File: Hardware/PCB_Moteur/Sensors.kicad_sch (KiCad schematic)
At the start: 19 parts, among them J18 Conn_01x04_Socket, J19 Conn_01x04_Socket, U7 INA125UA/2K5, U8 INA125UA/2K5, U9 MAX6612MXK

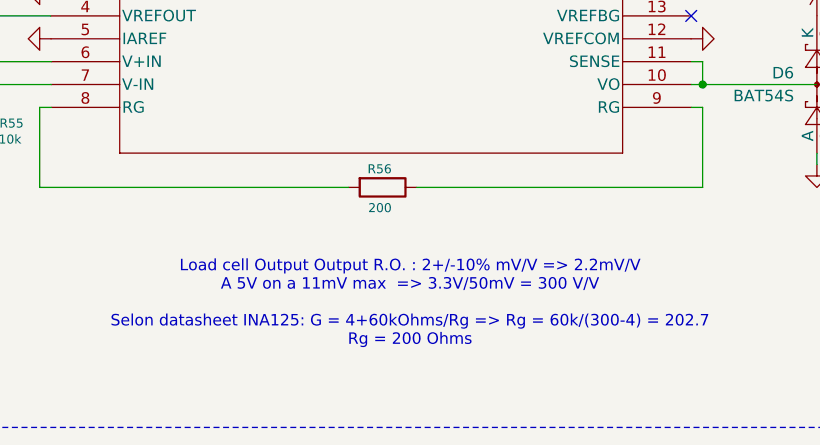
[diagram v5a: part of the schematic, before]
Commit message: wip : minor corrections and fix footprints except connectors
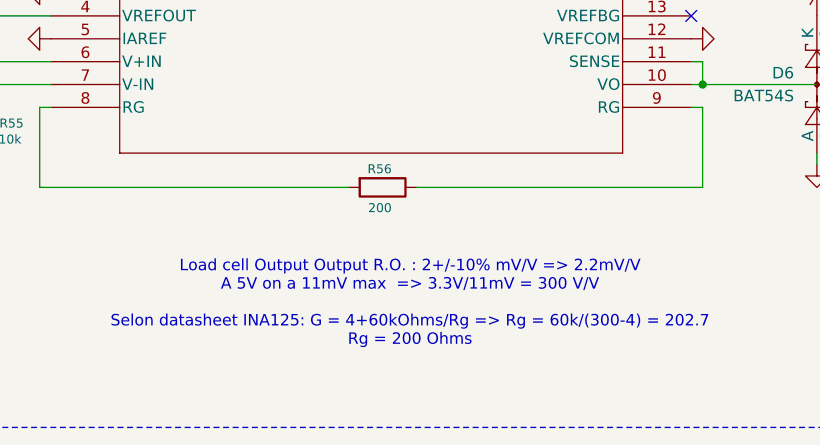
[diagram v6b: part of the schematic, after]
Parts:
- C44, C45, C46, C47, C48, C49: footprint (none) -> Capacitor_SMD:C_0805_2012Metric
- U7, U8: footprint D16 -> Package_SO:SOIC-16_3.9x9.9mm_P1.27mm
- U9: footprint MAX6612MXK:SOT65P210X110-5N -> Package_TO_SOT_SMD:SOT-353_SC-70-5
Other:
- note added: "Load cell Output Output R.O. : 2+/-10% mV/V => 2.2mV/V A 5V on a 11mV max => 3.3V/11mV = 300 V/V Selon datasheet INA125: G = 4+60kOhms/Rg => Rg = 60k/(300-4) = 202.7 Rg = 200 Ohms"
- note removed: "Load cell Output Output R.O. : 2+/-10% mV/V => 2.2mV/V A 5V on a 11mV max => 3.3V/50mV = 300 V/V Selon datasheet INA125: G = 4+60kOhms/Rg => Rg = 60k/(300-4) = 202.7 Rg = 200 Ohms"
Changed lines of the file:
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@@
 		)
 	)
-	(text "Load cell Output Output R.O. : 2+/-10% mV/V => 2.2mV/V\nA 5V on a 11mV max  => 3.3V/50mV = 300 V/V\n\nSelon datasheet INA125: G = 4+60kOhms/Rg => Rg = 60k/(300-4) = 202.7\nRg = 200 Ohms"
+	(text "Load cell Output Output R.O. : 2+/-10% mV/V => 2.2mV/V\nA 5V on a 11mV max  => 3.3V/11mV = 300 V/V\n\nSelon datasheet INA125: G = 4+60kOhms/Rg => Rg = 60k/(300-4) = 202.7\nRg = 200 Ohms"
 		(exclude_from_sim no)
 		(at 81.788 165.354 0)
@@
 			)
 		)
-		(property "Footprint" ""
+		(property "Footprint" "Capacitor_SMD:C_0805_2012Metric"
 			(at 140.6652 73.66 0)
 			(effects
@@
 			)
 		)
-		(property "Footprint" ""
+		(property "Footprint" "Capacitor_SMD:C_0805_2012Metric"
 			(at 266.7 33.3248 0)
 			(effects
@@
 			)
 		)
-		(property "Footprint" ""
+		(property "Footprint" "Capacitor_SMD:C_0805_2012Metric"
 			(at 258.7752 48.26 0)
 			(effects
@@
 			)
 		)
-		(property "Footprint" "MAX6612MXK:SOT65P210X110-5N"
+		(property "Footprint" "Package_TO_SOT_SMD:SOT-353_SC-70-5"
 			(at 240.03 44.45 0)
 			(effects
@@
 			)
 		)
-		(property "Footprint" ""
+		(property "Footprint" "Capacitor_SMD:C_0805_2012Metric"
 			(at 143.2052 148.59 0)
 			(effects
@@
 			)
 		)
-		(property "Footprint" "D16"
+		(property "Footprint" "Package_SO:SOIC-16_3.9x9.9mm_P1.27mm"
 			(at 41.91 125.73 0)
 			(effects
@@
 			)
 		)
-		(property "Footprint" ""
+		(property "Footprint" "Capacitor_SMD:C_0805_2012Metric"
 			(at 34.29 45.4152 0)
 			(effects
@@
 			)
 		)
-		(property "Footprint" "D16"
+		(property "Footprint" "Package_SO:SOIC-16_3.9x9.9mm_P1.27mm"
 			(at 43.18 50.8 0)
 			(effects
@@
 			)
 		)
-		(property "Footprint" ""
+		(property "Footprint" "Capacitor_SMD:C_0805_2012Metric"
 			(at 33.02 120.3452 0)
 			(effects

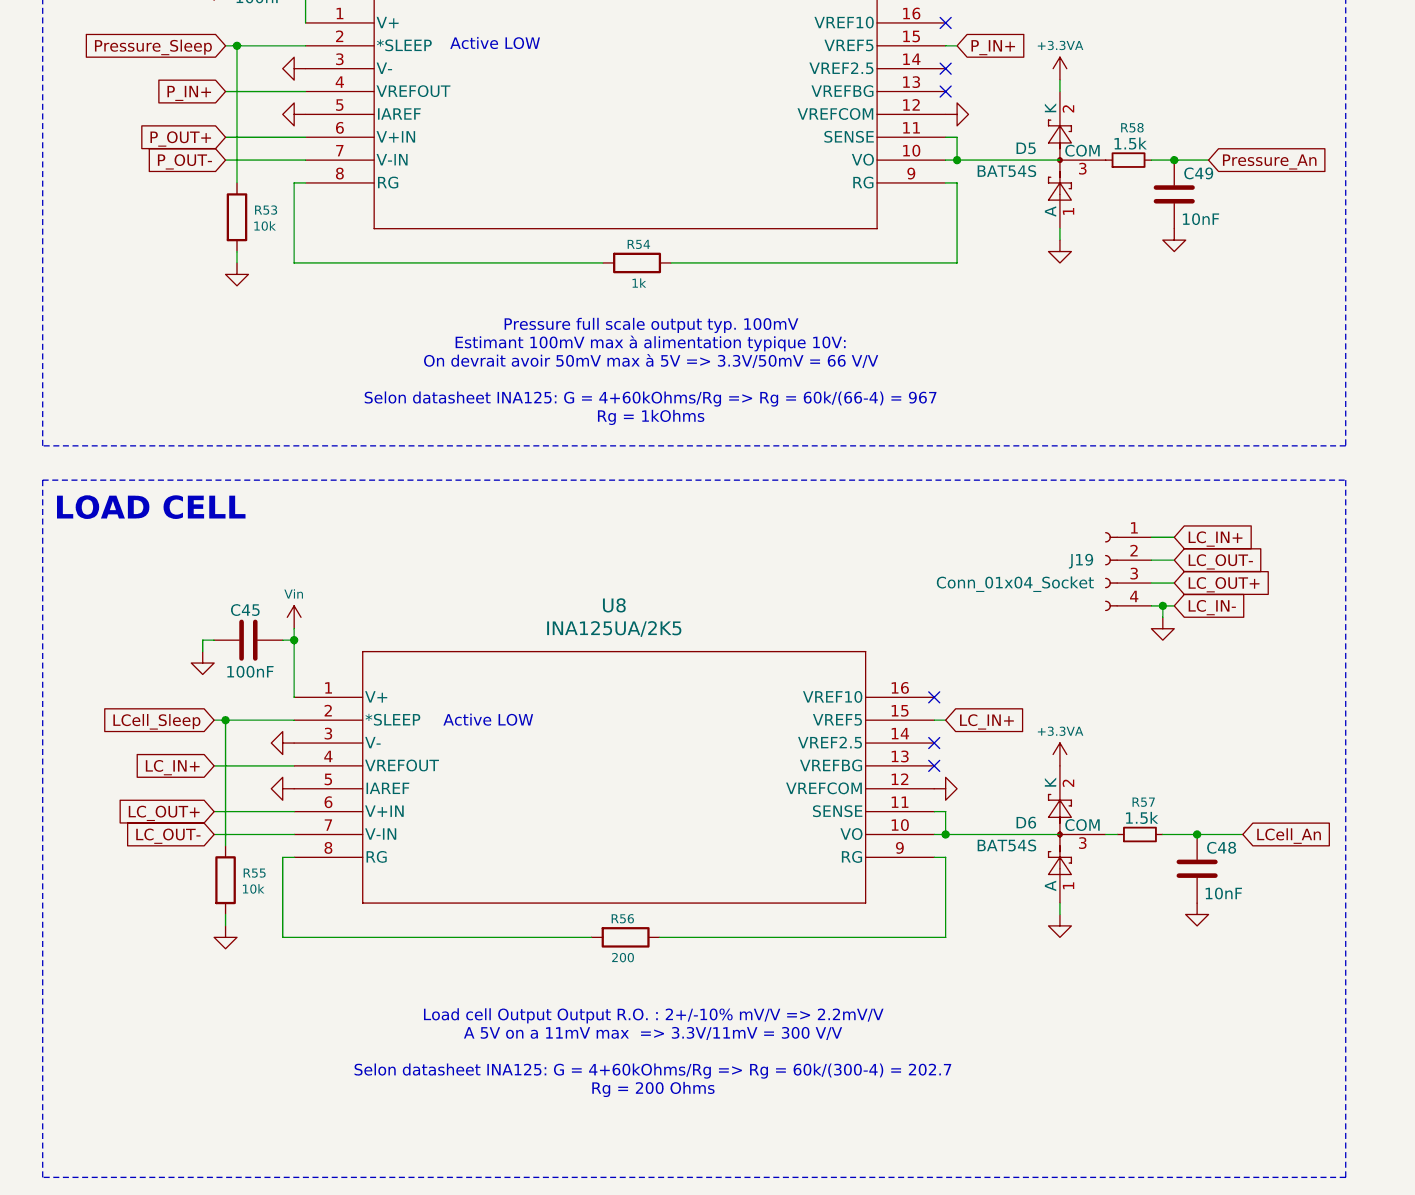
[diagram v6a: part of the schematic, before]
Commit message: fix: symbols refactorisation (footprint missing)
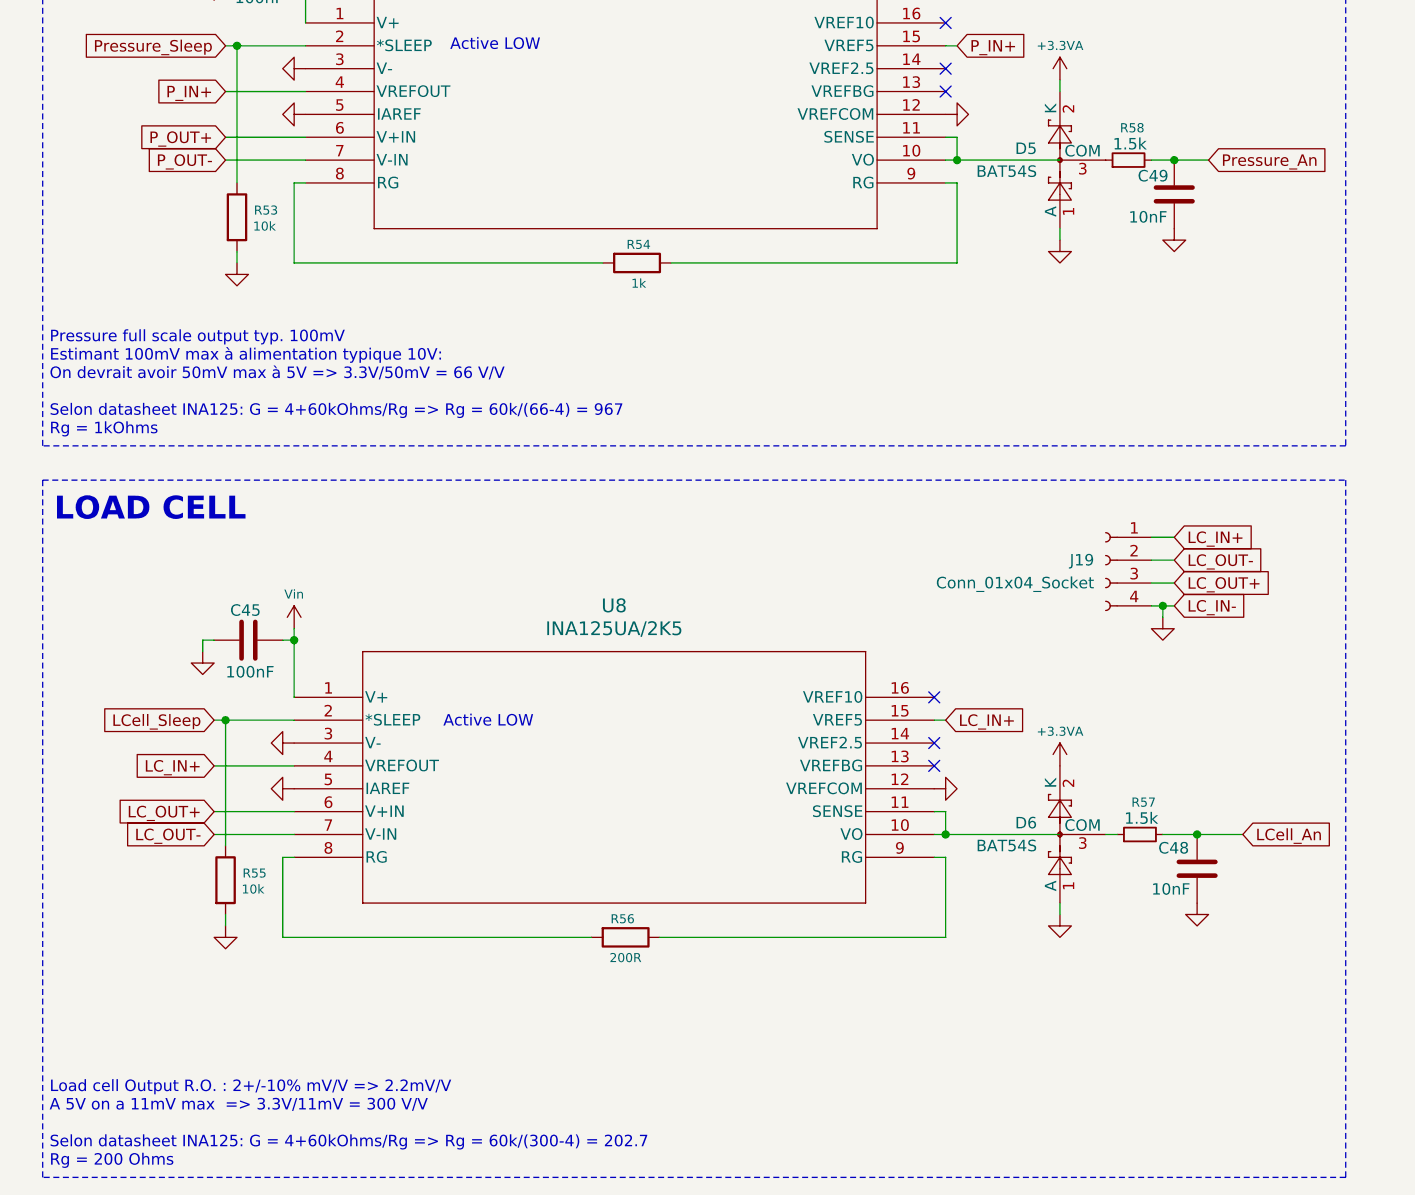
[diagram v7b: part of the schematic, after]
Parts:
- removed U7, U8: INA125UA/2K5, Package_SO:SOIC-16_3.9x9.9mm_P1.27mm, symbol 2026-01-14_14-23-56:INA125UA_2K5
- added U7, U8: INA125UA/2K5, D16, symbol pcb_moteur:INA125UA_2K5
- R56: value 200 -> 200R
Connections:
- net GND: now also U7.12 (VREFCOM), U7.3 (V-), U7.5 (IAREF), U8.12 (VREFCOM), U8.3 (V-), U8.5 (IAREF)
- net LC_IN+: now also U8.15 (VREF5), U8.4 (VREFOUT)
- net LC_OUT+: now also U8.6 (V+IN)
- net LC_OUT-: now also U8.7 (V-IN)
- net LCell_Sleep: now also U8.2 (*SLEEP)
- net P_IN+: now also U7.15 (VREF5), U7.4 (VREFOUT)
- net P_OUT+: now also U7.6 (V+IN)
- net P_OUT-: now also U7.7 (V-IN)
- net Pressure_Sleep: now also U7.2 (*SLEEP)
- net Vin: now also U7.1 (V+), U8.1 (V+)
- net at R56.1: now also U8.9 (RG)
- net at R56.2: now also U8.8 (RG)
- net at R54.2: now also U7.8 (RG)
- net at R54.1: now also U7.9 (RG)
- new net: U7.10 (VO), U7.11 (SENSE)
- new net: U8.10 (VO), U8.11 (SENSE)
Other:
- note added: "Load cell Output R.O. : 2+/-10% mV/V => 2.2mV/V A 5V on a 11mV max => 3.3V/11mV = 300 V/V Selon datasheet INA125: G = 4+60kOhms/Rg => Rg = 60k/(300-4) = 202.7 Rg = 200 Ohms"
- note removed: "Load cell Output Output R.O. : 2+/-10% mV/V => 2.2mV/V A 5V on a 11mV max => 3.3V/11mV = 300 V/V Selon datasheet INA125: G = 4+60kOhms/Rg => Rg = 60k/(300-4) = 202.7 Rg = 200 Ohms"
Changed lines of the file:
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@@
 		)
 	)
-	(text "Load cell Output Output R.O. : 2+/-10% mV/V => 2.2mV/V\nA 5V on a 11mV max  => 3.3V/11mV = 300 V/V\n\nSelon datasheet INA125: G = 4+60kOhms/Rg => Rg = 60k/(300-4) = 202.7\nRg = 200 Ohms"
+	(text "Load cell Output R.O. : 2+/-10% mV/V => 2.2mV/V\nA 5V on a 11mV max  => 3.3V/11mV = 300 V/V\n\nSelon datasheet INA125: G = 4+60kOhms/Rg => Rg = 60k/(300-4) = 202.7\nRg = 200 Ohms"
 		(exclude_from_sim no)
-		(at 81.788 165.354 0)
+		(at 14.732 173.228 0)
 		(effects
 			(font
 				(size 1.27 1.27)
 			)
+			(justify left)
 		)
 	)
 	(text "Pressure full scale output typ. 100mV\nEstimant 100mV max à alimentation typique 10V:\nOn devrait avoir 50mV max à 5V => 3.3V/50mV = 66 V/V\n\nSelon datasheet INA125: G = 4+60kOhms/Rg => Rg = 60k/(66-4) = 967\nRg = 1kOhms"
 		(exclude_from_sim no)
-		(at 81.534 89.662 0)
+		(at 14.732 90.932 0)
 		(effects
 			(font
 				(size 1.27 1.27)
 			)
+			(justify left)
 		)
 	)
@@
 		(dnp no)
 		(property "Reference" "C49"
-			(at 140.716 67.564 0)
+			(at 135.636 67.818 0)
 			(effects
 				(font
@@
 		)
 		(property "Value" "10nF"
-			(at 140.462 72.644 0)
+			(at 134.62 72.39 0)
 			(effects
 				(font
@@
 	)
 	(symbol
+		(lib_id "pcb_moteur:INA125UA_2K5")
+		(at 43.18 50.8 0)
+		(unit 1)
+		(exclude_from_sim no)
+		(in_bom yes)
+		(on_board yes)
+		(dnp no)
+		(fields_autoplaced yes)
+		(property "Reference" "U7"
+			(at 78.74 40.64 0)
+			(effects
+				(font
+					(size 1.524 1.524)
+				)
+			)
+		)
+		(property "Value" "INA125UA/2K5"
+			(at 78.74 43.18 0)
+			(effects
+				(font
+					(size 1.524 1.524)
+				)
+			)
+		)
+		(property "Footprint" "D16"
+			(at 43.18 50.8 0)
+			(effects
+				(font
+					(size 1.27 1.27)
+					(italic yes)
+				)
+				(hide yes)
+			)
+		)
+		(property "Datasheet" "https://www.ti.com/lit/gpn/ina125"
+			(at 43.18 50.8 0)
+			(effects
+				(font
+					(size 1.27 1.27)
+					(italic yes)
+				)
+				(hide yes)
+			)
+		)
+		(property "Description" ""
+			(at 43.18 50.8 0)
+			(effects
+				(font
+					(size 1.27 1.27)
+				)
+				(hide yes)
+			)
+		)
+		(pin "4"
+		)
+		(pin "1"
+		)
+		(pin "6"
+		)
+		(pin "2"
+		)
+		(pin "3"
+		)
+		(pin "5"
+		)
+		(pin "8"
+		)
+		(pin "10"
+		)
+		(pin "16"
+		)
+		(pin "14"
+		)
+		(pin "9"
+		)
+		(pin "7"
+		)
+		(pin "15"
+		)
+		(pin "11"
+		)
+		(pin "13"
+		)
+		(pin "12"
+		)
+		(instances
+			(project ""
+				(path "/b0d87684-7b1c-41d8-8358-755aa327573e/f31687d3-ca84-4d71-914a-32b6c2b363a9"
+					(reference "U7")
+					(unit 1)
+				)
+			)
+		)
+	)
+	(symbol
 		(lib_id "Device:C")
 		(at 262.89 34.29 90)
@@
 	)
 	(symbol
+		(lib_id "pcb_moteur:INA125UA_2K5")
+		(at 41.91 125.73 0)
+		(unit 1)
+		(exclude_from_sim no)
+		(in_bom yes)
+		(on_board yes)
+		(dnp no)
+		(fields_autoplaced yes)
+		(property "Reference" "U8"
+			(at 77.47 115.57 0)
+			(effects
+				(font
+					(size 1.524 1.524)
+				)
+			)
+		)
+		(property "Value" "INA125UA/2K5"
+			(at 77.47 118.11 0)
+			(effects
+				(font
+					(size 1.524 1.524)
+				)
+			)
+		)
+		(property "Footprint" "D16"
+			(at 41.91 125.73 0)
+			(effects
+				(font
+					(size 1.27 1.27)
+					(italic yes)
+				)
+				(hide yes)
+			)
+		)
+		(property "Datasheet" "https://www.ti.com/lit/gpn/ina125"
+			(at 41.91 125.73 0)
+			(effects
+				(font
+					(size 1.27 1.27)
+					(italic yes)
+				)
+				(hide yes)
+			)
+		)
+		(property "Description" ""
+			(at 41.91 125.73 0)
+			(effects
+				(font
+					(size 1.27 1.27)
+				)
+				(hide yes)
+			)
+		)
+		(pin "4"
+		)
+		(pin "1"
+		)
+		(pin "6"
+		)
+		(pin "2"
+		)
+		(pin "3"
+		)
+		(pin "5"
+		)
+		(pin "8"
+		)
+		(pin "10"
+		)
+		(pin "16"
+		)
+		(pin "14"
+		)
+		(pin "9"
+		)
+		(pin "7"
+		)
+		(pin "15"
+		)
+		(pin "11"
+		)
+		(pin "13"
+		)
+		(pin "12"
+		)
+		(instances
+			(project "PCB_moteur"
+				(path "/b0d87684-7b1c-41d8-8358-755aa327573e/f31687d3-ca84-4d71-914a-32b6c2b363a9"
+					(reference "U8")
+					(unit 1)
+				)
+			)
+		)
+	)
+	(symbol
 		(lib_id "power:GND")
 		(at 127 74.93 0)
@@
 		(dnp no)
 		(property "Reference" "C48"
-			(at 143.256 142.494 0)
+			(at 137.922 142.494 0)
 			(effects
 				(font
@@
 		)
 		(property "Value" "10nF"
-			(at 143.002 147.574 0)
+			(at 137.16 147.066 0)
 			(effects
 				(font
@@
 			)
 		)
-		(property "Value" "200"
-			(at 79.756 154.686 90)
+		(property "Value" "200R"
+			(at 80.518 154.686 90)
 			(effects
 				(font
@@
 	)
 	(symbol
-		(lib_id "2026-01-14_14-23-56:INA125UA_2K5")
-		(at 41.91 125.73 0)
-		(unit 1)
-		(exclude_from_sim no)
-		(in_bom yes)
-		(on_board yes)
-		(dnp no)
-		(fields_autoplaced yes)
-		(property "Reference" "U8"
-			(at 77.47 115.57 0)
-			(effects
-				(font
-					(size 1.524 1.524)
-				)
-			)
-		)
-		(property "Value" "INA125UA/2K5"
-			(at 77.47 118.11 0)
-			(effects
-				(font
-					(size 1.524 1.524)
-				)
-			)
-		)
-		(property "Footprint" "Package_SO:SOIC-16_3.9x9.9mm_P1.27mm"
-			(at 41.91 125.73 0)
-			(effects
-				(font
-					(size 1.27 1.27)
-					(italic yes)
-				)
-				(hide yes)
-			)
-		)
-		(property "Datasheet" "https://www.ti.com/lit/gpn/ina125"
-			(at 41.91 125.73 0)
-			(effects
-				(font
-					(size 1.27 1.27)
-					(italic yes)
-				)
-				(hide yes)
-			)
-		)
-		(property "Description" ""
-			(at 41.91 125.73 0)
-			(effects
-				(font
-					(size 1.27 1.27)
-				)
-				(hide yes)
-			)
-		)
-		(pin "12"
-		)
-		(pin "11"
-		)
-		(pin "9"
-		)
-		(pin "16"
-		)
-		(pin "14"
-		)
-		(pin "8"
-		)
-		(pin "7"
-		)
-		(pin "10"
-		)
-		(pin "15"
-		)
-		(pin "13"
-		)
-		(pin "4"
-		)
-		(pin "5"
-		)
-		(pin "6"
-		)
-		(pin "1"
-		)
-		(pin "2"
-		)
-		(pin "3"
-		)
-		(instances
-			(project "PCB_moteur"
-				(path "/b0d87684-7b1c-41d8-8358-755aa327573e/f31687d3-ca84-4d71-914a-32b6c2b363a9"
-					(reference "U8")
-					(unit 1)
-				)
-			)
-		)
-	)
-	(symbol
 		(lib_id "power:GND")
 		(at 34.29 151.13 0)
@@
 					(unit 1)
 				)
-			)
-		)
-	)
-	(symbol
-		(lib_id "2026-01-14_14-23-56:INA125UA_2K5")
-		(at 43.18 50.8 0)
-		(unit 1)
-		(exclude_from_sim no)
-		(in_bom yes)
-		(on_board yes)
-		(dnp no)
-		(fields_autoplaced yes)
-		(property "Reference" "U7"
-			(at 78.74 40.64 0)
-			(effects
-				(font
-					(size 1.524 1.524)
-				)
-			)
-		)
-		(property "Value" "INA125UA/2K5"
-			(at 78.74 43.18 0)
-			(effects
-				(font
-					(size 1.524 1.524)
-				)
-			)
-		)
-		(property "Footprint" "Package_SO:SOIC-16_3.9x9.9mm_P1.27mm"
-			(at 43.18 50.8 0)
-			(effects
-				(font
-					(size 1.27 1.27)
-					(italic yes)
-				)
-				(hide yes)
-			)
-		)
-		(property "Datasheet" "https://www.ti.com/lit/gpn/ina125"
-			(at 43.18 50.8 0)
-			(effects
-				(font
-					(size 1.27 1.27)
-					(italic yes)
-				)
-				(hide yes)
-			)
-		)
-		(property "Description" ""
-			(at 43.18 50.8 0)
-			(effects
-				(font
-					(size 1.27 1.27)
-				)
-				(hide yes)
-			)
-		)
-		(pin "12"
-		)
-		(pin "11"
-		)
-		(pin "9"
-		)
-		(pin "16"
-		)
-		(pin "14"
-		)
-		(pin "8"
-		)
-		(pin "7"
-		)
-		(pin "10"
-		)
-		(pin "15"
-		)
-		(pin "13"
-		)
-		(pin "4"
-		)
-		(pin "5"
-		)
-		(pin "6"
-		)
-		(pin "1"
-		)
-		(pin "2"
-		)
-		(pin "3"
-		)
-		(instances
-			(project "PCB_moteur"
-				(path "/b0d87684-7b1c-41d8-8358-755aa327573e/f31687d3-ca84-4d71-914a-32b6c2b363a9"
-					(reference "U7")
-					(unit 1)
-				)
